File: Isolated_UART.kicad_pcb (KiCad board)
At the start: 2 copper layers, 32.4 x 52.7 mm, 32 parts, among them J2 USB_C_Receptacle_USB2.0, J3 Conn_01x10_Male, J4 Conn_01x03_Male, U1 USBLC6-2SC6, U2 ADuM1401xRW, U3 FT231XS-R, U4 ADuM1402xRW, U5 AP2127N-3.3

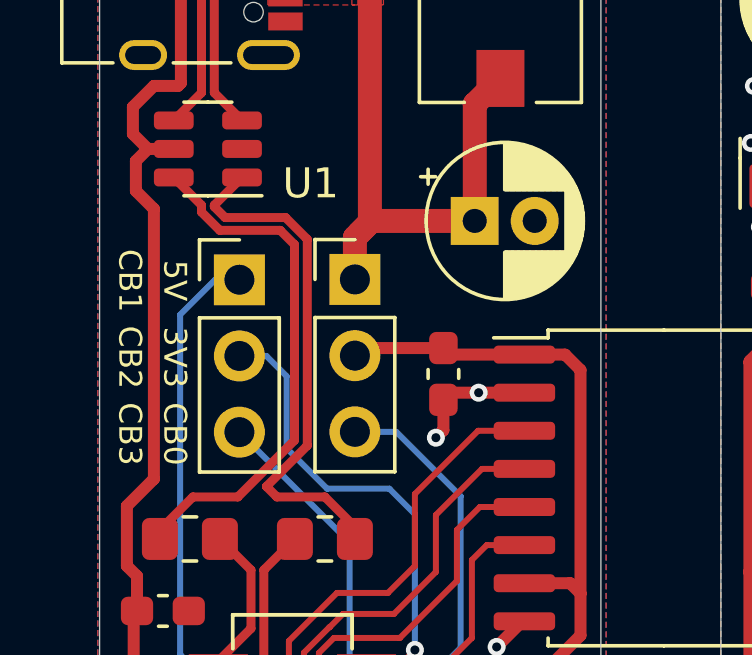
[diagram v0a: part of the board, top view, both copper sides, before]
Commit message: Revised the schematic for clarity
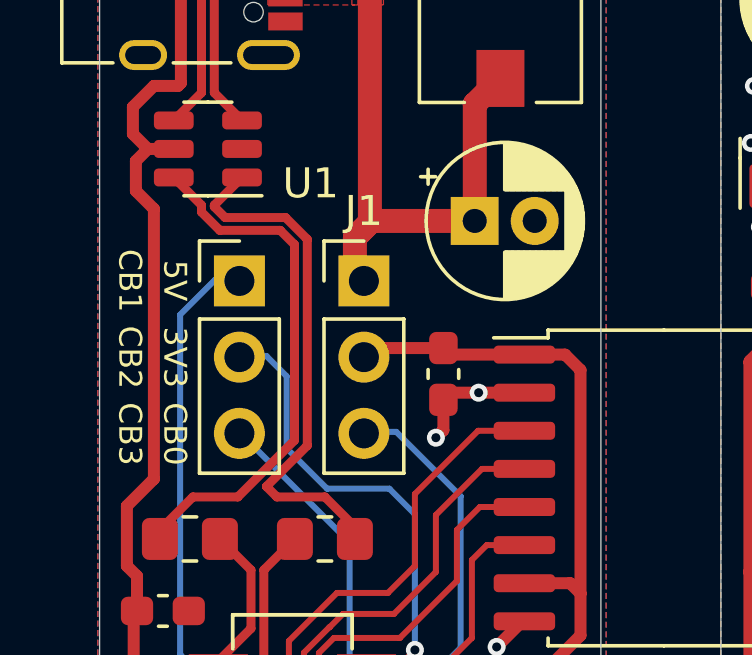
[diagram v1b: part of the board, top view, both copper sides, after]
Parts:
- removed Je: Conn_01x03_Male, Connector_PinHeader_2.54mm:PinHeader_1x03_P2.54mm_Vertical
- added J1: Conn_01x03_Male, Connector_PinHeader_2.54mm:PinHeader_1x03_P2.54mm_Vertical, F.Cu at (169.3, 58.7)
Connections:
- net +3VA renamed +3V3A
